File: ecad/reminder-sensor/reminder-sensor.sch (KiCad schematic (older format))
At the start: 6 parts

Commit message: Changed sensor pinout to 3 pin connector
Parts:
- removed H? (x2): MountingHole, symbol Mechanical:MountingHole
- removed R?: 10k, Resistor_THT:R_Axial_DIN0204_L3.6mm_D1.6mm_P5.08mm_Horizontal, symbol Device:R_Small_US
- J1: renamed from J?; value Conn_01x04_Male -> Conn_01x03_Male; symbol Connector:Conn_01x04_Male -> Connector:Conn_01x03_Male
- gave numbers to parts that had none: 2
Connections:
- net +3V3 is gone; now on net OUTPUT: J1.2 (Pin_2)
- net GND: now also J1.3 (Pin_3); no longer J1.4 (Pin_4)
- net OUTPUT: no longer J1.3 (Pin_3)
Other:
- note added: "Connector"
- note added: "Sensor"
- moved on the sheet: R1, U1
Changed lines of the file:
@@
 $EndDescr
 $Comp
-L SENSOR_PROX_QRD:QRD1113GR U?
+L SENSOR_PROX_QRD:QRD1113GR U1
 U 1 1 6085AF80
-P 5250 3500
-F 0 "U?" H 5250 3817 50  0000 C CNN
-F 1 "QRD1113GR" H 5250 3726 50  0000 C CNN
-F 2 "OptoDevice:Everlight_ITR8307F43" H 5250 3300 50  0001 C CNN
-F 3 "https://everlighteurope.com/index.php?controller=attachment&id_attachment=5385" H 5250 3600 50  0001 C CNN
-	1    5250 3500
+P 6500 3950
+F 0 "U1" H 6500 4267 50  0000 C CNN
+F 1 "QRD1113GR" H 6500 4176 50  0000 C CNN
+F 2 "OptoDevice:Everlight_ITR8307F43" H 6500 3750 50  0001 C CNN
+F 3 "https://everlighteurope.com/index.php?controller=attachment&id_attachment=5385" H 6500 4050 50  0001 C CNN
+	1    6500 3950
 	1    0    0    -1
 $EndComp
 $Comp
-L power:+3.3V #PWR?
-U 1 1 60863FAA
-P 5700 3150
-F 0 "#PWR?" H 5700 3000 50  0001 C CNN
-F 1 "+3.3V" H 5715 3323 50  0000 C CNN
-F 2 "" H 5700 3150 50  0001 C CNN
-F 3 "" H 5700 3150 50  0001 C CNN
-	1    5700 3150
+L power:GND #PWR0101
+U 1 1 608660BA
+P 6800 4200
+F 0 "#PWR0101" H 6800 3950 50  0001 C CNN
+F 1 "GND" H 6805 4027 50  0000 C CNN
+F 2 "" H 6800 4200 50  0001 C CNN
+F 3 "" H 6800 4200 50  0001 C CNN
+	1    6800 4200
 	1    0    0    -1
 $EndComp
 $Comp
-L power:GND #PWR?
-U 1 1 608660BA
-P 5550 3750
-F 0 "#PWR?" H 5550 3500 50  0001 C CNN
-F 1 "GND" H 5555 3577 50  0000 C CNN
-F 2 "" H 5550 3750 50  0001 C CNN
-F 3 "" H 5550 3750 50  0001 C CNN
-	1    5550 3750
+L power:GND #PWR0102
+U 1 1 6086650D
+P 6200 4200
+F 0 "#PWR0102" H 6200 3950 50  0001 C CNN
+F 1 "GND" H 6205 4027 50  0000 C CNN
+F 2 "" H 6200 4200 50  0001 C CNN
+F 3 "" H 6200 4200 50  0001 C CNN
+	1    6200 4200
+	1    0    0    -1
+$EndComp
+Wire Wire Line
+	6200 4200 6200 4050
+Wire Wire Line
+	6800 4200 6800 4050
+$Comp
+L Device:R_Small_US R1
+U 1 1 60868A1D
+P 6100 3700
+F 0 "R1" H 6033 3746 50  0000 R CNN
+F 1 "160" H 6033 3655 50  0000 R CNN
+F 2 "Resistor_THT:R_Axial_DIN0204_L3.6mm_D1.6mm_P5.08mm_Horizontal" H 6100 3700 50  0001 C CNN
+F 3 "~" H 6100 3700 50  0001 C CNN
+	1    6100 3700
 	1    0    0    -1
 $EndComp
 $Comp
-L power:GND #PWR?
-U 1 1 6086650D
-P 4950 3750
-F 0 "#PWR?" H 4950 3500 50  0001 C CNN
-F 1 "GND" H 4955 3577 50  0000 C CNN
-F 2 "" H 4950 3750 50  0001 C CNN
-F 3 "" H 4950 3750 50  0001 C CNN
-	1    4950 3750
+L power:+5V #PWR0103
+U 1 1 60869558
+P 6100 3600
+F 0 "#PWR0103" H 6100 3450 50  0001 C CNN
+F 1 "+5V" H 6115 3773 50  0000 C CNN
+F 2 "" H 6100 3600 50  0001 C CNN
+F 3 "" H 6100 3600 50  0001 C CNN
+	1    6100 3600
 	1    0    0    -1
 $EndComp
 Wire Wire Line
-	4950 3750 4950 3600
+	6100 3800 6100 3850
 Wire Wire Line
-	5550 3750 5550 3600
+	6100 3850 6200 3850
 $Comp
-L Device:R_Small_US R?
-U 1 1 6086832A
-P 5700 3250
-F 0 "R?" H 5768 3296 50  0000 L CNN
-F 1 "10k" H 5768 3205 50  0000 L CNN
-F 2 "Resistor_THT:R_Axial_DIN0204_L3.6mm_D1.6mm_P5.08mm_Horizontal" H 5700 3250 50  0001 C CNN
-F 3 "~" H 5700 3250 50  0001 C CNN
-	1    5700 3250
+L Connector:Conn_01x03_Male J1
+U 1 1 6086CBB9
+P 4300 3950
+F 0 "J1" H 4408 4231 50  0000 C CNN
+F 1 "Conn_01x03_Male" H 4408 4140 50  0000 C CNN
+F 2 "" H 4300 3950 50  0001 C CNN
+F 3 "~" H 4300 3950 50  0001 C CNN
+	1    4300 3950
 	1    0    0    -1
 $EndComp
 $Comp
-L Device:R_Small_US R?
-U 1 1 60868A1D
-P 4850 3250
-F 0 "R?" H 4783 3296 50  0000 R CNN
-F 1 "160" H 4783 3205 50  0000 R CNN
-F 2 "Resistor_THT:R_Axial_DIN0204_L3.6mm_D1.6mm_P5.08mm_Horizontal" H 4850 3250 50  0001 C CNN
-F 3 "~" H 4850 3250 50  0001 C CNN
-	1    4850 3250
+L power:+5V #PWR0104
+U 1 1 6087060B
+P 4900 3700
+F 0 "#PWR0104" H 4900 3550 50  0001 C CNN
+F 1 "+5V" H 4915 3873 50  0000 C CNN
+F 2 "" H 4900 3700 50  0001 C CNN
+F 3 "" H 4900 3700 50  0001 C CNN
+	1    4900 3700
 	1    0    0    -1
 $EndComp
 $Comp
-L power:+5V #PWR?
-U 1 1 60869558
-P 4850 3150
-F 0 "#PWR?" H 4850 3000 50  0001 C CNN
-F 1 "+5V" H 4865 3323 50  0000 C CNN
-F 2 "" H 4850 3150 50  0001 C CNN
-F 3 "" H 4850 3150 50  0001 C CNN
-	1    4850 3150
+L power:GND #PWR0105
+U 1 1 60871256
+P 4900 4150
+F 0 "#PWR0105" H 4900 3900 50  0001 C CNN
+F 1 "GND" H 4905 3977 50  0000 C CNN
+F 2 "" H 4900 4150 50  0001 C CNN
+F 3 "" H 4900 4150 50  0001 C CNN
+	1    4900 4150
 	1    0    0    -1
 $EndComp
 Wire Wire Line
-	4850 3350 4850 3400
+	4900 3700 4900 3850
 Wire Wire Line
-	4850 3400 4950 3400
+	4900 3850 4500 3850
 Wire Wire Line
-	5550 3400 5700 3400
+	4900 3950 4500 3950
+Text Label 4900 3950 0    50   ~ 0
+OUTPUT
+Text Label 7000 3850 0    50   ~ 0
+OUTPUT
 Wire Wire Line
-	5700 3400 5700 3350
+	6800 3850 7000 3850
+Wire Wire Line
+	4900 4150 4900 4050
+Wire Wire Line
+	4900 4050 4500 4050
+Text Notes 6250 3150 0    100  ~ 20
+Sensor
+Text Notes 4400 3150 0    100  ~ 20
+Connector
 $Comp
-L Mechanical:MountingHole H?
-U 1 1 6086B06B
-P 7200 3200
-F 0 "H?" H 7300 3246 50  0000 L CNN
-F 1 "MountingHole" H 7300 3155 50  0000 L CNN
-F 2 "" H 7200 3200 50  0001 C CNN
-F 3 "~" H 7200 3200 50  0001 C CNN
-	1    7200 3200
+L power:PWR_FLAG #FLG0101
+U 1 1 608BC905
+P 3000 2550
+F 0 "#FLG0101" H 3000 2625 50  0001 C CNN
+F 1 "PWR_FLAG" H 3000 2723 50  0000 C CNN
+F 2 "" H 3000 2550 50  0001 C CNN
+F 3 "~" H 3000 2550 50  0001 C CNN
+	1    3000 2550
+	-1   0    0    1
+$EndComp
+$Comp
+L power:PWR_FLAG #FLG0102
+U 1 1 608BD77D
+P 2600 2550
+F 0 "#FLG0102" H 2600 2625 50  0001 C CNN
+F 1 "PWR_FLAG" H 2600 2723 50  0000 C CNN
+F 2 "" H 2600 2550 50  0001 C CNN
+F 3 "~" H 2600 2550 50  0001 C CNN
+	1    2600 2550
 	1    0    0    -1
 $EndComp
 $Comp
-L Mechanical:MountingHole H?
-U 1 1 6086BAE7
-P 7200 3600
-F 0 "H?" H 7300 3646 50  0000 L CNN
-F 1 "MountingHole" H 7300 3555 50  0000 L CNN
-F 2 "" H 7200 3600 50  0001 C CNN
-F 3 "~" H 7200 3600 50  0001 C CNN
-	1    7200 3600
+L power:GND #PWR0106
+U 1 1 608BDBD9
+P 2600 2550
+F 0 "#PWR0106" H 2600 2300 50  0001 C CNN
+F 1 "GND" H 2605 2377 50  0000 C CNN
+F 2 "" H 2600 2550 50  0001 C CNN
+F 3 "" H 2600 2550 50  0001 C CNN
+	1    2600 2550
 	1    0    0    -1
 $EndComp
 $Comp
-L Connector:Conn_01x04_Male J?
-U 1 1 6086CBB9
-P 2450 3450
-F 0 "J?" H 2558 3731 50  0000 C CNN
-F 1 "Conn_01x04_Male" H 2558 3640 50  0000 C CNN
-F 2 "" H 2450 3450 50  0001 C CNN
-F 3 "~" H 2450 3450 50  0001 C CNN
-	1    2450 3450
+L power:+5V #PWR0107
+U 1 1 608BE1F7
+P 3000 2550
+F 0 "#PWR0107" H 3000 2400 50  0001 C CNN
+F 1 "+5V" H 3015 2723 50  0000 C CNN
+F 2 "" H 3000 2550 50  0001 C CNN
+F 3 "" H 3000 2550 50  0001 C CNN
+	1    3000 2550
 	1    0    0    -1
 $EndComp
-$Comp
-L power:+5V #PWR?
-U 1 1 6087060B
-P 3050 3200
-F 0 "#PWR?" H 3050 3050 50  0001 C CNN
-F 1 "+5V" H 3065 3373 50  0000 C CNN
-F 2 "" H 3050 3200 50  0001 C CNN
-F 3 "" H 3050 3200 50  0001 C CNN
-	1    3050 3200
-	1    0    0    -1
-$EndComp
-$Comp
-L power:+3.3V #PWR?
-U 1 1 60870AF6
-P 3350 3200
-F 0 "#PWR?" H 3350 3050 50  0001 C CNN
-F 1 "+3.3V" H 3365 3373 50  0000 C CNN
-F 2 "" H 3350 3200 50  0001 C CNN
-F 3 "" H 3350 3200 50  0001 C CNN
-	1    3350 3200
-	1    0    0    -1
-$EndComp
-$Comp
-L power:GND #PWR?
-U 1 1 60871256
-P 3050 3800
-F 0 "#PWR?" H 3050 3550 50  0001 C CNN
-F 1 "GND" H 3055 3627 50  0000 C CNN
-F 2 "" H 3050 3800 50  0001 C CNN
-F 3 "" H 3050 3800 50  0001 C CNN
-	1    3050 3800
-	1    0    0    -1
-$EndComp
-Wire Wire Line
-	3050 3200 3050 3350
-Wire Wire Line
-	3050 3350 2650 3350
-Wire Wire Line
-	3350 3200 3350 3450
-Wire Wire Line
-	3350 3450 2650 3450
-Wire Wire Line
-	2650 3650 3050 3650
-Wire Wire Line
-	3050 3650 3050 3800
-Text Label 3300 3550 0    50   ~ 0
-OUTPUT
-Wire Wire Line
-	3300 3550 2650 3550
-Text Label 6000 3400 0    50   ~ 0
-OUTPUT
-Wire Wire Line
-	6000 3400 5700 3400
-Connection ~ 5700 3400
 $EndSCHEMATC

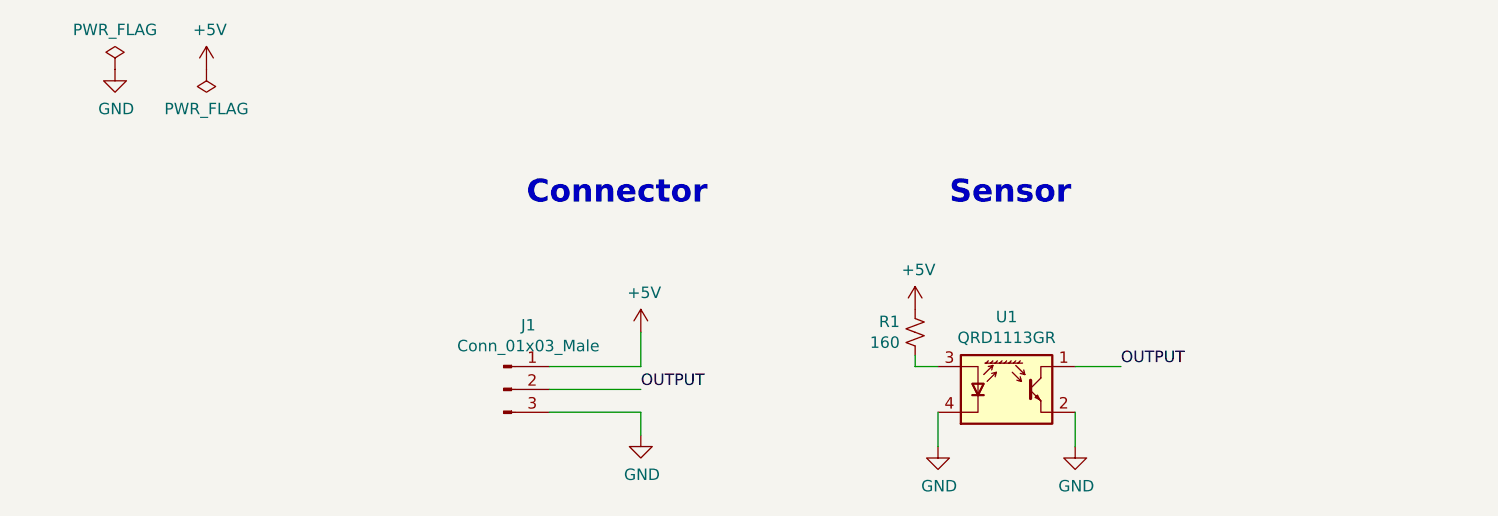
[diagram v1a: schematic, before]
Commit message: Finished sensor board schematic
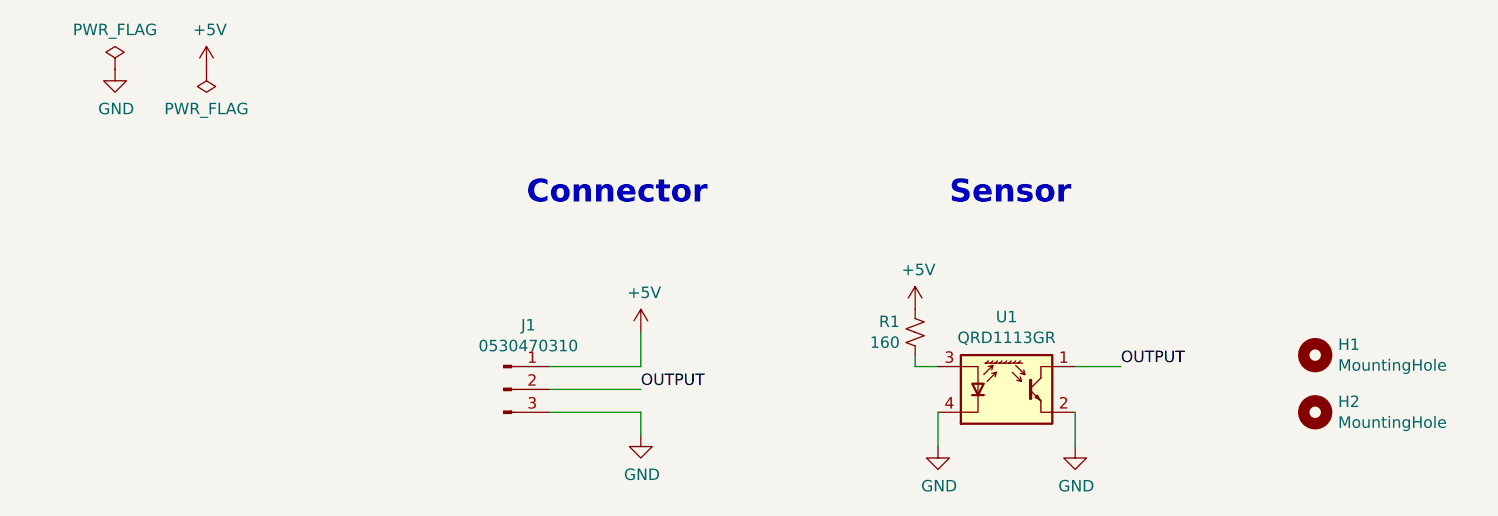
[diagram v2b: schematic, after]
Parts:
- added H1, H2: MountingHole, MountingHole:MountingHole_2.2mm_M2, symbol Mechanical:MountingHole
- J1: value Conn_01x03_Male -> 0530470310; footprint (none) -> Connector_Molex:Molex_PicoBlade_53047-0310_1x03_P1.25mm_Vertical
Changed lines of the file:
@@
 $EndDescr
-$Comp
-L SENSOR_PROX_QRD:QRD1113GR U1
-U 1 1 6085AF80
-P 6500 3950
-F 0 "U1" H 6500 4267 50  0000 C CNN
-F 1 "QRD1113GR" H 6500 4176 50  0000 C CNN
-F 2 "OptoDevice:Everlight_ITR8307F43" H 6500 3750 50  0001 C CNN
-F 3 "https://everlighteurope.com/index.php?controller=attachment&id_attachment=5385" H 6500 4050 50  0001 C CNN
-	1    6500 3950
-	1    0    0    -1
-$EndComp
 $Comp
 L power:GND #PWR0101
@@
 P 4300 3950
 F 0 "J1" H 4408 4231 50  0000 C CNN
-F 1 "Conn_01x03_Male" H 4408 4140 50  0000 C CNN
-F 2 "" H 4300 3950 50  0001 C CNN
+F 1 "0530470310" H 4408 4140 50  0000 C CNN
+F 2 "Connector_Molex:Molex_PicoBlade_53047-0310_1x03_P1.25mm_Vertical" H 4300 3950 50  0001 C CNN
 F 3 "~" H 4300 3950 50  0001 C CNN
 	1    4300 3950
@@
 	1    0    0    -1
 $EndComp
+$Comp
+L SENSOR_PROX_QRD:QRD1113GR U1
+U 1 1 6085AF80
+P 6500 3950
+F 0 "U1" H 6500 4267 50  0000 C CNN
+F 1 "QRD1113GR" H 6500 4176 50  0000 C CNN
+F 2 "OptoDevice:Everlight_ITR8307F43" H 6500 3750 50  0001 C CNN
+F 3 "https://everlighteurope.com/index.php?controller=attachment&id_attachment=5385" H 6500 4050 50  0001 C CNN
+	1    6500 3950
+	1    0    0    -1
+$EndComp
+$Comp
+L Mechanical:MountingHole H1
+U 1 1 60916ABE
+P 7850 3800
+F 0 "H1" H 7950 3846 50  0000 L CNN
+F 1 "MountingHole" H 7950 3755 50  0000 L CNN
+F 2 "MountingHole:MountingHole_2.2mm_M2" H 7850 3800 50  0001 C CNN
+F 3 "~" H 7850 3800 50  0001 C CNN
+	1    7850 3800
+	1    0    0    -1
+$EndComp
+$Comp
+L Mechanical:MountingHole H2
+U 1 1 60917130
+P 7850 4050
+F 0 "H2" H 7950 4096 50  0000 L CNN
+F 1 "MountingHole" H 7950 4005 50  0000 L CNN
+F 2 "MountingHole:MountingHole_2.2mm_M2" H 7850 4050 50  0001 C CNN
+F 3 "~" H 7850 4050 50  0001 C CNN
+	1    7850 4050
+	1    0    0    -1
+$EndComp

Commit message: Finished routing, silkscreen details.
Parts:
- R1: footprint Resistor_THT:R_Axial_DIN0204_L3.6mm_D1.6mm_P5.08mm_Horizontal -> Resistor_SMD:R_1206_3216Metric
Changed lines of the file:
@@
 F 0 "R1" H 6033 3746 50  0000 R CNN
 F 1 "160" H 6033 3655 50  0000 R CNN
-F 2 "Resistor_THT:R_Axial_DIN0204_L3.6mm_D1.6mm_P5.08mm_Horizontal" H 6100 3700 50  0001 C CNN
+F 2 "Resistor_SMD:R_1206_3216Metric" H 6100 3700 50  0001 C CNN
 F 3 "~" H 6100 3700 50  0001 C CNN
 	1    6100 3700
